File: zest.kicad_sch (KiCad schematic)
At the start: 7 parts

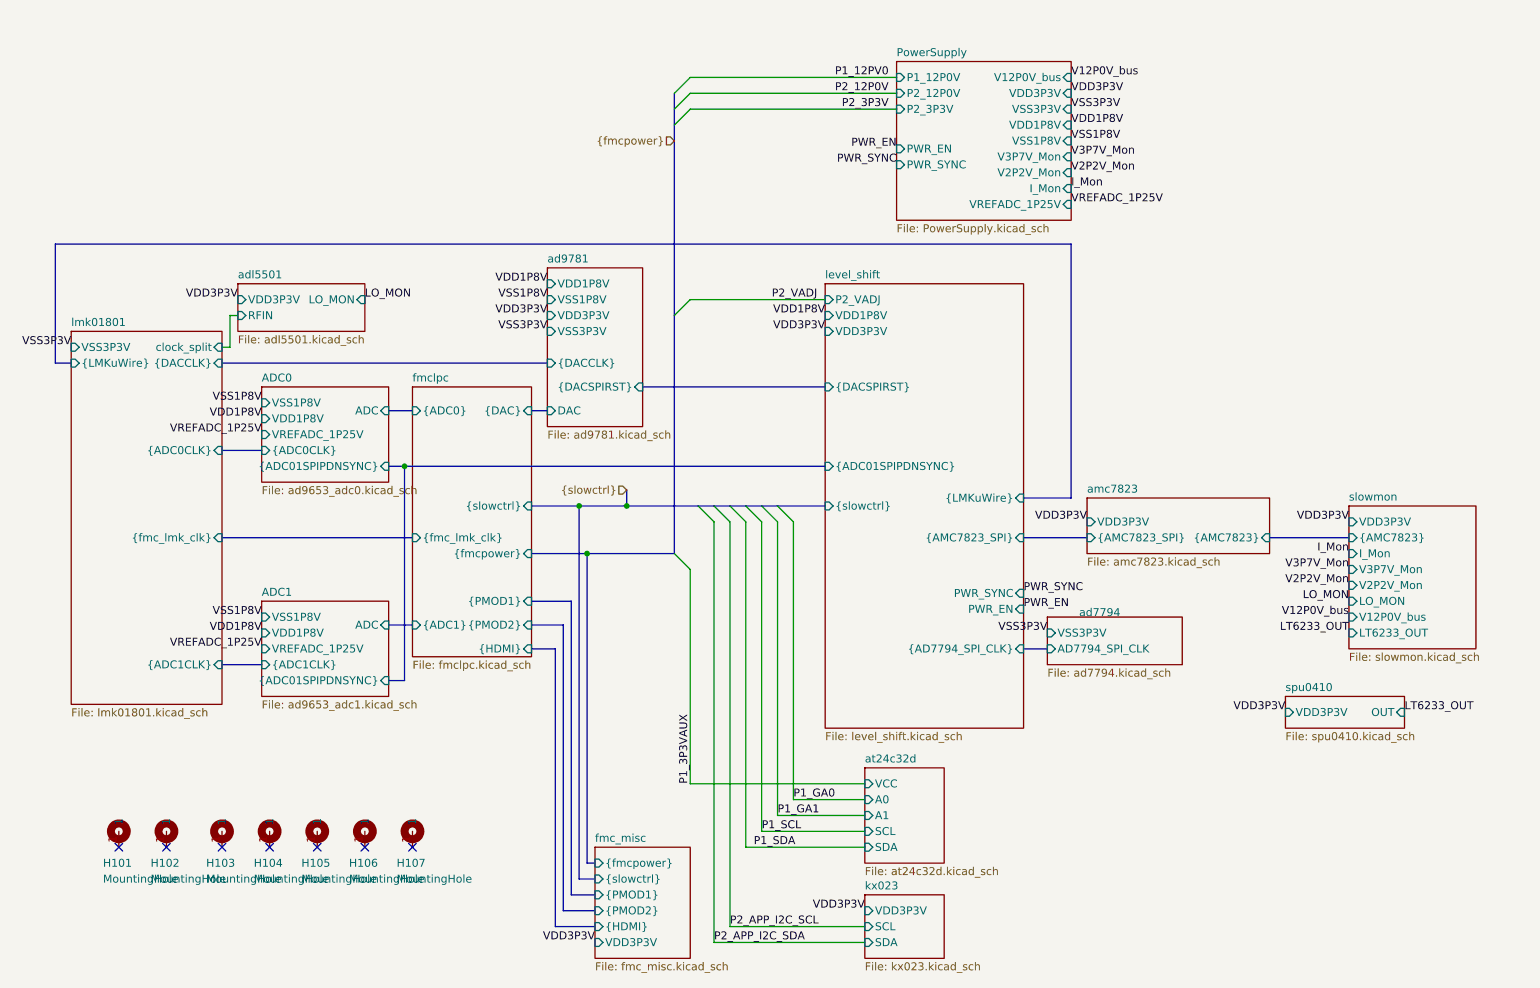
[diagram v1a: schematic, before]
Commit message: Added -3.3V supply, buffer amplifier, and single-to-differential op-amp circuit
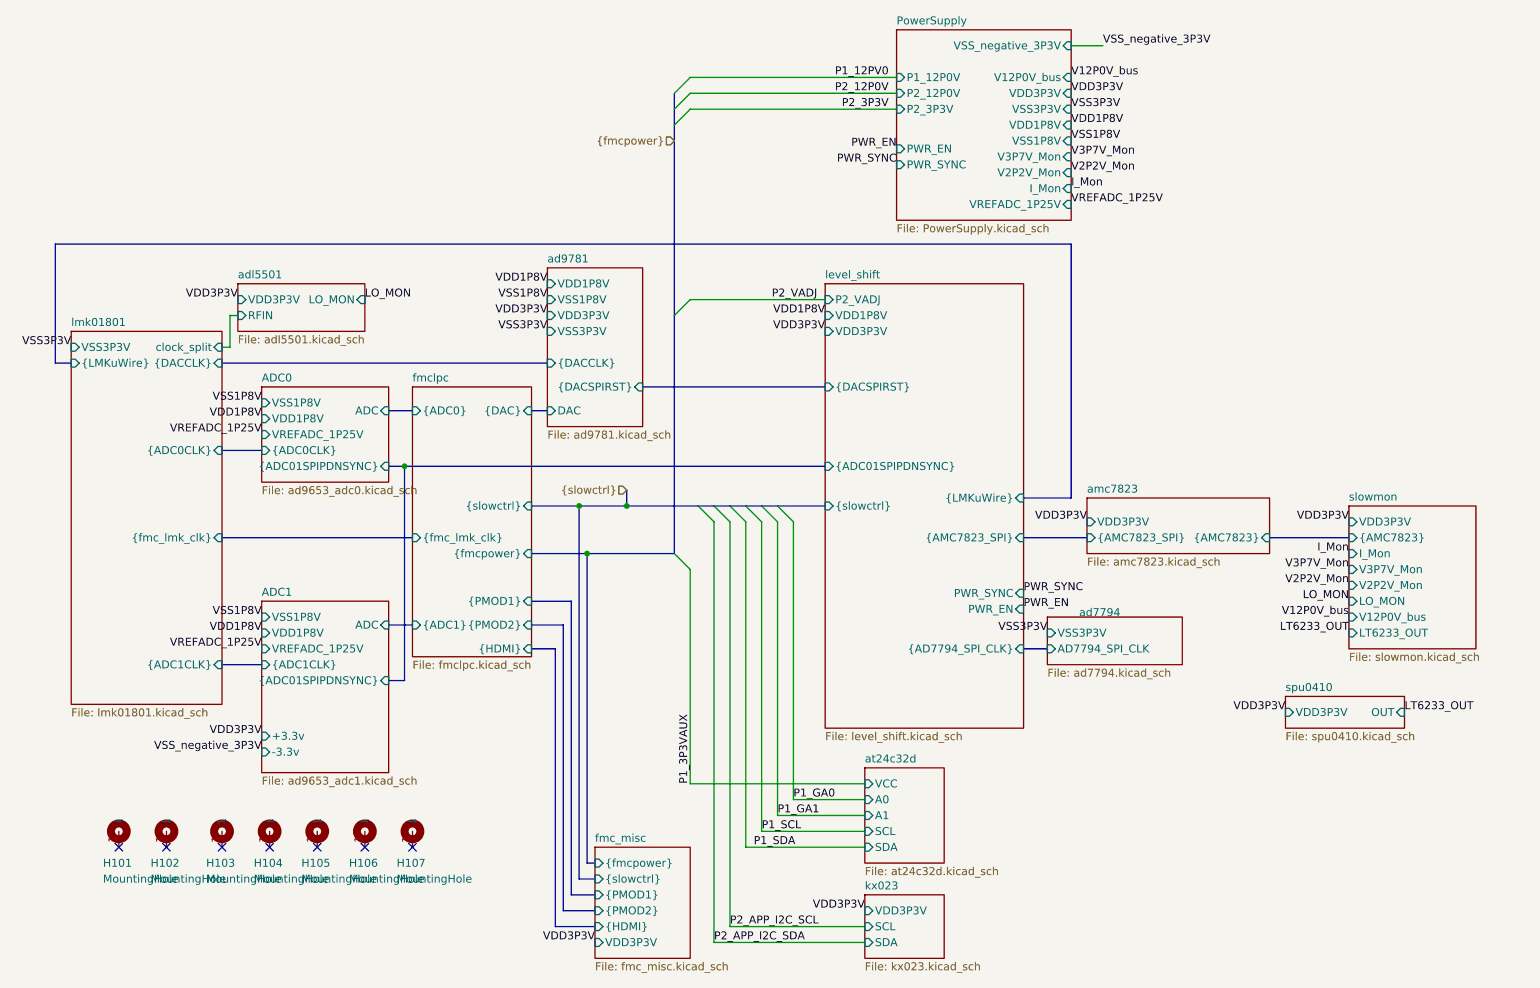
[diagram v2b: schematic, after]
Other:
- sheet ADC1 ports: added +3.3v, -3.3v; removed none
- sheet PowerSupply ports: added VSS_negative_3P3V; removed none
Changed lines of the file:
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@@
+		)
+	)
+	(wire
+		(pts
+			(xy 190.5 16.51) (xy 195.58 16.51)
+		)
+		(stroke
+			(width 0)
+			(type default)
 		)
 	)
@@
 		)
 	)
+	(label "VSS_negative_3P3V"
+		(at 60.96 129.54 180)
+		(fields_autoplaced yes)
+		(effects
+			(font
+				(size 1.27 1.27)
+			)
+			(justify right bottom)
+		)
+	)
 	(label "VREFADC_1P25V"
 		(at 60.96 78.74 180)
@@
 		)
 	)
+	(label "VSS_negative_3P3V"
+		(at 195.58 16.51 0)
+		(fields_autoplaced yes)
+		(effects
+			(font
+				(size 1.27 1.27)
+			)
+			(justify left bottom)
+		)
+	)
 	(label "VDD1P8V"
 		(at 190.5 29.21 0)
@@
 	(label "V2P2V_Mon"
 		(at 234.95 102.87 180)
+		(fields_autoplaced yes)
+		(effects
+			(font
+				(size 1.27 1.27)
+			)
+			(justify right bottom)
+		)
+	)
+	(label "VDD3P3V"
+		(at 60.96 127 180)
 		(fields_autoplaced yes)
 		(effects
@@
 	(sheet
 		(at 60.96 105.41)
-		(size 20.32 15.24)
+		(size 20.32 27.432)
 		(fields_autoplaced yes)
 		(stroke
@@
 		)
 		(property "Sheetfile" "ad9653_adc1.kicad_sch"
-			(at 60.96 121.2346 0)
+			(at 60.96 133.4266 0)
 			(effects
 				(font
@@
 				)
 				(justify right)
+			)
+		)
+		(pin "+3.3v" input
+			(at 60.96 127 180)
+			(effects
+				(font
+					(size 1.27 1.27)
+				)
+				(justify left)
+			)
+		)
+		(pin "-3.3v" input
+			(at 60.96 129.54 180)
+			(effects
+				(font
+					(size 1.27 1.27)
+				)
+				(justify left)
 			)
 		)
@@
 	)
 	(sheet
-		(at 162.56 19.05)
-		(size 27.94 25.4)
+		(at 162.56 13.97)
+		(size 27.94 30.48)
 		(fields_autoplaced yes)
 		(stroke
@@
 		)
 		(property "Sheetname" "PowerSupply"
-			(at 162.56 18.3384 0)
+			(at 162.56 13.2584 0)
 			(effects
 				(font
@@
 			(effects
 				(font
+					(size 1.27 1.27)
+				)
+				(justify right)
+			)
+		)
+		(pin "VSS_negative_3P3V" input
+			(at 190.5 16.51 0)
+			(effects
+				(font

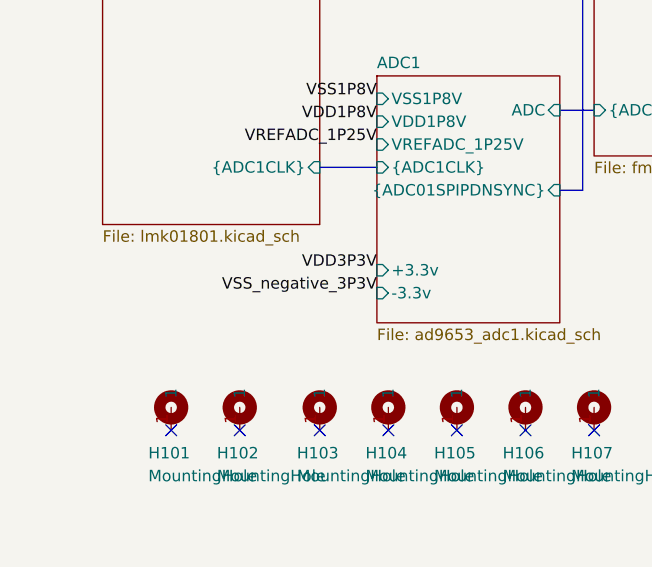
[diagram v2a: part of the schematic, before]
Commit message: Revert FMC connector edge cuts to main version, replace synchronized DC-DC converter with LM2776 (2MHz unsynchronized)
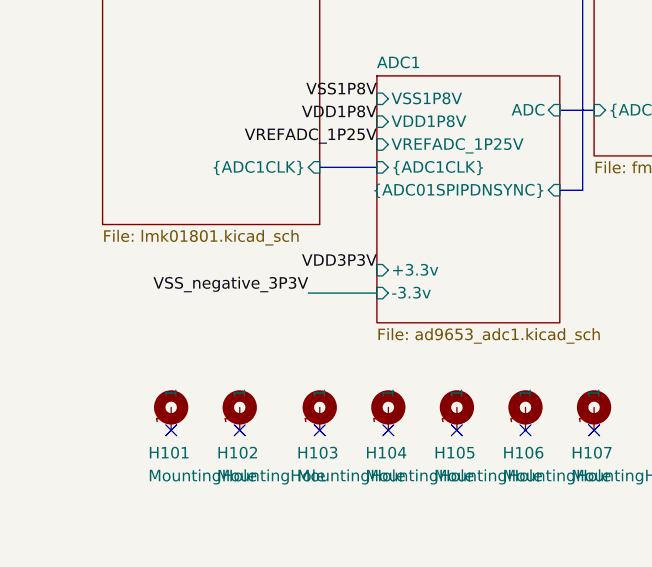
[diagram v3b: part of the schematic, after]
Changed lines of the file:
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@@
+		)
+	)
+	(wire
+		(pts
+			(xy 53.34 129.54) (xy 60.96 129.54)
+		)
+		(stroke
+			(width 0)
+			(type default)
 		)
 	)
@@
 	)
 	(label "VSS_negative_3P3V"
-		(at 60.96 129.54 180)
-		(fields_autoplaced yes)
-		(effects
+		(at 53.34 129.54 180)
+		(fields_autoplaced yes)
+		(effects
